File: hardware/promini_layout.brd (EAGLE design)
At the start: 6 parts

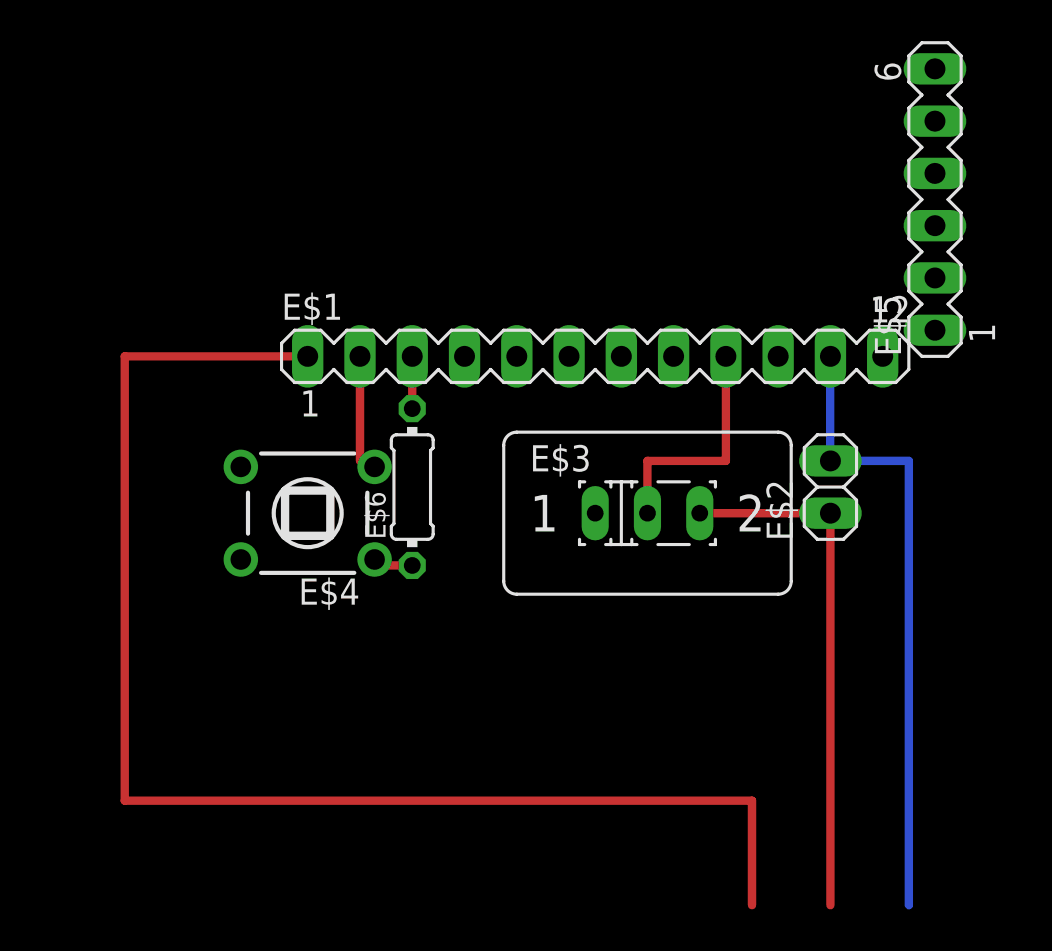
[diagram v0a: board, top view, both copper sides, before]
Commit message: Corrected hardware layout - added photos of the finished product - tested and working
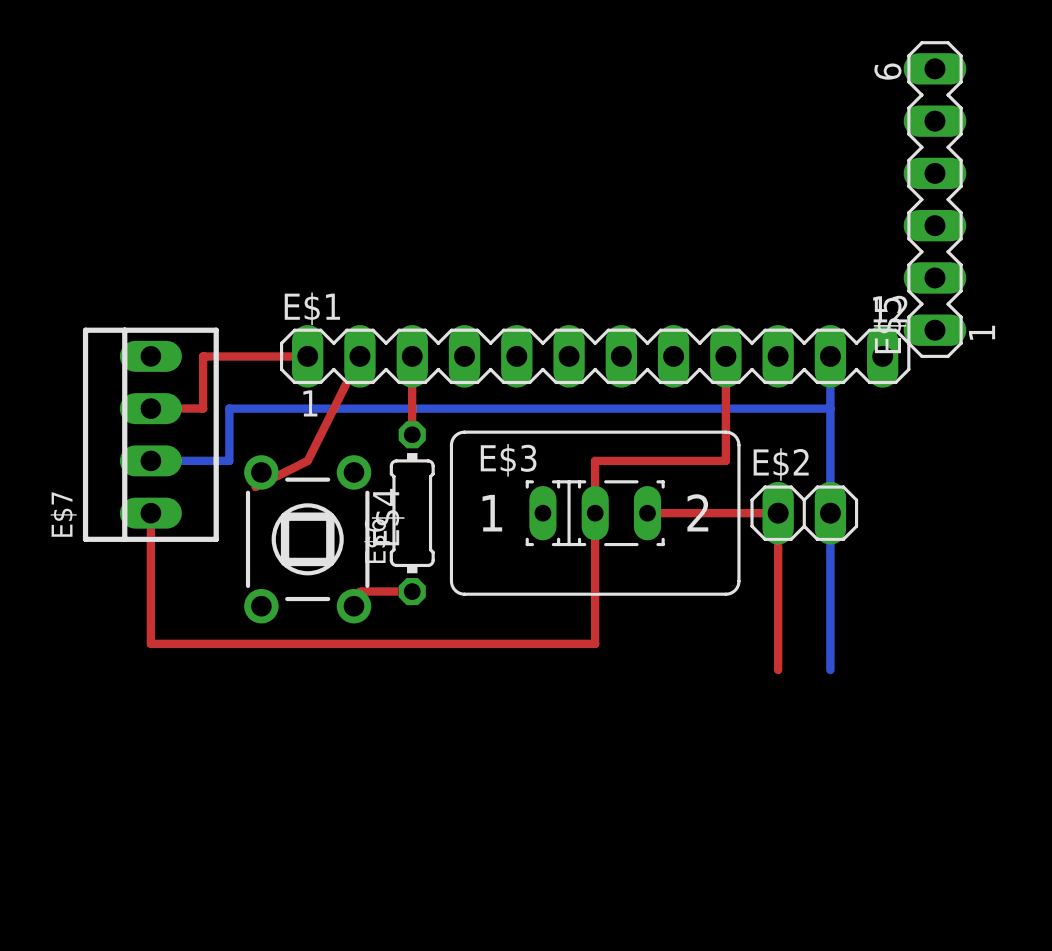
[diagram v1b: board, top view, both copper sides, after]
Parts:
- added E$7: (no value), con-molex:22-23-2041
- moved E$3 2.54 mm to (47.0, 53.3)
- moved E$2 1.80 mm to (57.1, 53.3), turned to 0 degrees
- moved E$4 1.27 mm to (33.0, 52.1), turned to 180 degrees
- moved E$6 1.27 mm to (38.1, 53.3)
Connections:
- removed net S$7: E$1.1
- new net S$8: E$1.11, E$2.2, E$7.2
- net S$1: now also E$1.1, E$7.3; no longer E$1.11, E$2.2
- net S$3: now also E$7.1
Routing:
- net S$7: track 66.0 -> 0.00 mm
- net S$8: track 0.00 -> 50.8 mm
- net S$3: track 11.4 -> 48.3 mm
- net S$1: track 30.5 -> 10.2 mm
- net S$2: track 25.4 -> 14.0 mm
- net S$4: track 5.08 -> 8.52 mm
- net S$6: track 2.54 -> 3.81 mm
- net S$5: track 1.27 -> 2.54 mm
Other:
- board text added: "data"
- board text removed: "data vcc gnd"
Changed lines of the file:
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@@
 <text x="33.02" y="78.74" size="1.778" layer="51">Pro mini 3v3 8MHz, atmega328</text>
 <rectangle x1="31.75" y1="59.69" x2="64.77" y2="77.47" layer="51"/>
-<text x="64.77" y="53.34" size="1.778" layer="51">JST 2pin skt</text>
+<text x="60.96" y="53.34" size="1.778" layer="51">JST 2pin skt</text>
 <text x="67.31" y="68.58" size="1.778" layer="51">Leave room for FTDI serial lead here</text>
-<text x="43.18" y="46.99" size="1.778" layer="51">power switch</text>
-<text x="29.21" y="45.72" size="1.778" layer="51">button</text>
-<text x="52.07" y="31.75" size="1.778" layer="51">data vcc gnd</text>
-<text x="52.07" y="27.94" size="1.778" layer="51">to neopixels</text>
+<text x="39.37" y="41.91" size="1.778" layer="51">power switch</text>
+<text x="26.67" y="41.91" size="1.778" layer="51">button</text>
+<text x="16.51" y="58.42" size="1.778" layer="51">data</text>
+<text x="6.35" y="49.53" size="1.778" layer="51">to neopixels</text>
 <text x="33.02" y="63.5" size="1.778" layer="18" rot="R90">10</text>
 <text x="35.56" y="63.5" size="1.778" layer="18" rot="R90">11</text>
@@
 <text x="53.34" y="63.5" size="1.778" layer="18" rot="R90">vcc</text>
 <text x="58.42" y="63.5" size="1.778" layer="18" rot="R90">gnd</text>
-<text x="64.77" y="49.53" size="1.778" layer="51">3-5V in</text>
+<text x="60.96" y="49.53" size="1.778" layer="51">3-5V in</text>
+<text x="16.51" y="55.88" size="1.778" layer="51">gnd</text>
+<text x="16.51" y="53.34" size="1.778" layer="51">vcc</text>
 </plain>
 <attributes>
@@
 </autorouter>
 <elements>
-<element name="E$3" library="switch" package="M251" value="" x="49.53" y="53.34"/>
+<element name="E$3" library="switch" package="M251" value="" x="46.99" y="53.34"/>
 <element name="E$1" library="con-lstb" package="MA12-1" value="" x="46.99" y="60.96"/>
-<element name="E$2" library="pinhead" package="1X02" value="" x="58.42" y="54.61" rot="R90"/>
-<element name="E$4" library="switch" package="TL1105T" value="" x="33.02" y="53.34" rot="R90"/>
+<element name="E$2" library="pinhead" package="1X02" value="" x="57.15" y="53.34"/>
+<element name="E$4" library="switch" package="TL1105T" value="" x="33.02" y="52.07" rot="R180"/>
 <element name="E$5" library="con-lstb" package="MA06-1" value="" x="63.5" y="68.58" rot="R90"/>
-<element name="E$6" library="eagle-ltspice" package="0204/7" value="1k" x="38.1" y="54.61" rot="R90"/>
+<element name="E$6" library="eagle-ltspice" package="0204/7" value="1k" x="38.1" y="53.34" rot="R90"/>
+<element name="E$7" library="con-molex" package="22-23-2041" value="" x="25.4" y="57.15" rot="R90"/>
 </elements>
 <signals>
-<signal name="S$1">
+<signal name="S$8">
+<contactref element="E$1" pad="11"/>
 <contactref element="E$2" pad="2"/>
-<contactref element="E$1" pad="11"/>
-<wire x1="58.42" y1="55.88" x2="58.42" y2="60.96" width="0.4064" layer="16"/>
-<wire x1="58.42" y1="55.88" x2="62.23" y2="55.88" width="0.4064" layer="16"/>
-<wire x1="62.23" y1="55.88" x2="62.23" y2="34.29" width="0.4064" layer="16"/>
+<wire x1="58.42" y1="53.34" x2="58.42" y2="58.42" width="0.4064" layer="16"/>
+<wire x1="58.42" y1="58.42" x2="58.42" y2="60.96" width="0.4064" layer="16"/>
+<wire x1="58.42" y1="53.34" x2="58.42" y2="45.72" width="0.4064" layer="16"/>
+<wire x1="58.42" y1="58.42" x2="29.21" y2="58.42" width="0.4064" layer="16"/>
+<wire x1="29.21" y1="58.42" x2="29.21" y2="55.88" width="0.4064" layer="16"/>
+<contactref element="E$7" pad="2"/>
+<wire x1="29.21" y1="55.88" x2="25.4" y2="55.88" width="0.4064" layer="16"/>
 </signal>
 <signal name="S$2">
 <contactref element="E$2" pad="1"/>
 <contactref element="E$3" pad="3"/>
-<wire x1="58.42" y1="53.34" x2="52.07" y2="53.34" width="0.4064" layer="1"/>
-<wire x1="58.42" y1="53.34" x2="58.42" y2="34.29" width="0.4064" layer="1"/>
+<wire x1="55.88" y1="53.34" x2="49.53" y2="53.34" width="0.4064" layer="1"/>
+<wire x1="55.88" y1="53.34" x2="55.88" y2="45.72" width="0.4064" layer="1"/>
 </signal>
 <signal name="S$3">
 <contactref element="E$3" pad="2"/>
-<wire x1="49.53" y1="53.34" x2="49.53" y2="55.88" width="0.4064" layer="1"/>
+<wire x1="46.99" y1="53.34" x2="46.99" y2="55.88" width="0.4064" layer="1"/>
 <contactref element="E$1" pad="9"/>
-<wire x1="49.53" y1="55.88" x2="53.34" y2="55.88" width="0.4064" layer="1"/>
+<wire x1="46.99" y1="55.88" x2="53.34" y2="55.88" width="0.4064" layer="1"/>
 <wire x1="53.34" y1="55.88" x2="53.34" y2="60.96" width="0.4064" layer="1"/>
+<wire x1="46.99" y1="53.34" x2="46.99" y2="46.99" width="0.4064" layer="1"/>
+<wire x1="46.99" y1="46.99" x2="25.4" y2="46.99" width="0.4064" layer="1"/>
+<contactref element="E$7" pad="1"/>
+<wire x1="25.4" y1="46.99" x2="25.4" y2="53.34" width="0.4064" layer="1"/>
 </signal>
 <signal name="S$4">
 <contactref element="E$1" pad="2"/>
-<wire x1="35.56" y1="60.96" x2="35.56" y2="55.88" width="0.4064" layer="1"/>
+<wire x1="35.56" y1="60.96" x2="33.02" y2="55.88" width="0.4064" layer="1"/>
+<wire x1="30.48" y1="54.61" x2="33.02" y2="55.88" width="0.4064" layer="1"/>
 </signal>
 <signal name="S$5">
 <contactref element="E$6" pad="1"/>
-<wire x1="36.83" y1="50.8" x2="38.1" y2="50.8" width="0.4064" layer="1"/>
+<wire x1="35.56" y1="49.53" x2="38.1" y2="49.53" width="0.4064" layer="1"/>
 </signal>
 <signal name="S$6">
 <contactref element="E$6" pad="2"/>
 <contactref element="E$1" pad="3"/>
-<wire x1="38.1" y1="58.42" x2="38.1" y2="60.96" width="0.4064" layer="1"/>
-</signal>
-<signal name="S$7">
+<wire x1="38.1" y1="57.15" x2="38.1" y2="60.96" width="0.4064" layer="1"/>
+</signal>
+<signal name="S$1">
 <contactref element="E$1" pad="1"/>
-<wire x1="33.02" y1="60.96" x2="24.13" y2="60.96" width="0.4064" layer="1"/>
-<wire x1="24.13" y1="60.96" x2="24.13" y2="39.37" width="0.4064" layer="1"/>
-<wire x1="24.13" y1="39.37" x2="54.61" y2="39.37" width="0.4064" layer="1"/>
-<wire x1="54.61" y1="39.37" x2="54.61" y2="34.29" width="0.4064" layer="1"/>
+<wire x1="33.02" y1="60.96" x2="27.94" y2="60.96" width="0.4064" layer="1"/>
+<wire x1="27.94" y1="60.96" x2="27.94" y2="58.42" width="0.4064" layer="1"/>
+<contactref element="E$7" pad="3"/>
+<wire x1="27.94" y1="58.42" x2="25.4" y2="58.42" width="0.4064" layer="1"/>
 </signal>
 </signals>
